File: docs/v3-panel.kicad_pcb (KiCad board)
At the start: 2 copper layers, 20 x 128.5 mm, 0 parts

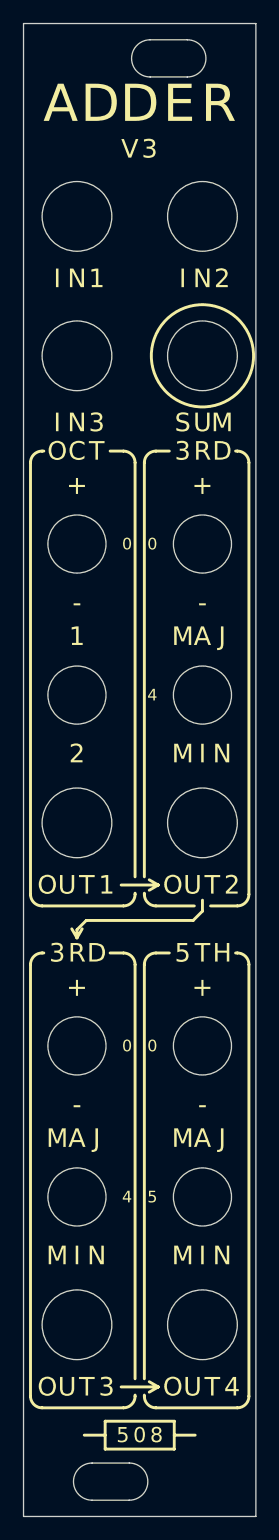
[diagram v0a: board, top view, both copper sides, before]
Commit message: Narrow the column pitch to 10.4 so part bodies clear the board edge
The DPDT selector is 9.10 mm wide once rotated for a vertical throw, so two of
them occupy 18.2 mm of a 20 mm panel - 1.8 mm of slack for everything else. At
the old 10.8 pitch their bodies, and the 9.00 mm jack bodies, overhung a 19 mm
PCB by about 0.45 mm a side.

The fix trades against panel legibility, because the detent mark sits between a
toggle nut and its box edge, and moving a column inward closes that gap:

  pitch 10.8   marks 0.25 mm   board must be 19.90 mm
  pitch 10.6   marks 0.20 mm   board must be 19.70 mm
  pitch 10.4   marks 0.15 mm   board must be 19.50 mm
  pitch 10.0   marks 0.05 mm   - unmanufacturable

10.4 is the balance point: 19.5 mm is an ordinary 4 HP board width where 19.9
is at the limit, and 0.15 mm is the usual fab silkscreen minimum. My first
attempt went to 10.0 on a mistaken reading - I had measured the channel between
the two nuts rather than the nut-to-box strip the marks actually live in, and
the panel's own clearance check caught it at 0.05 mm.

Board is now 19.6 x 111.5 mm with every body inside it, the sixteen
panel-defined parts re-placed on the new columns, and the README hole schedule
and clearance figures brought up to date.

Panel DRC 0 violations, schematic ERC 0 errors 0 warnings, and the board's
silk_edge_clearance warnings are gone.

Co-Authored-By: Claude Opus 5 <noreply@anthropic.com>
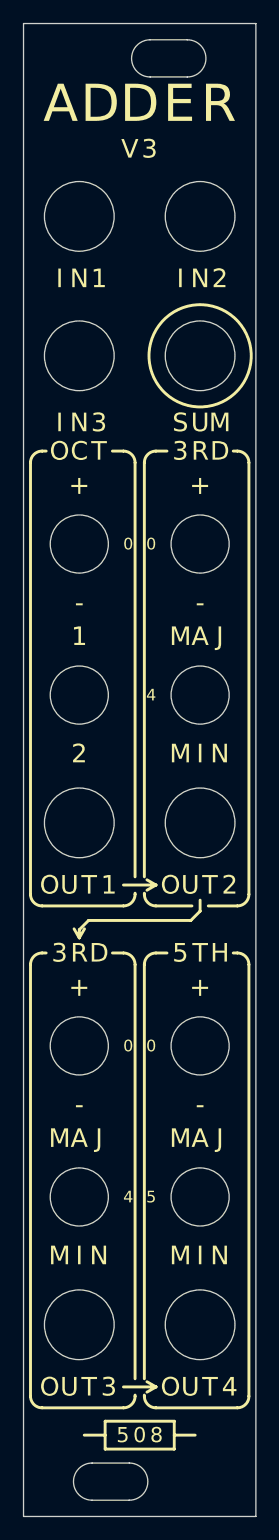
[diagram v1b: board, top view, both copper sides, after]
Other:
- outline, holes or cut-outs redrawn
